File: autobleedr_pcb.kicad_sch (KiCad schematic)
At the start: 21 parts, among them J1 Barrel_Jack, J10 XT60 Connector, J11 Conn_01x02_Pin, J13 Screw_Terminal_01x08, J2 Conn_01x01_Pin, J4 Conn_01x13_Pin, J5 Conn_01x13_Pin, J7 Screw_Terminal_01x02, J8 Conn_01x02_Pin, J9 Conn_01x02_Pin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

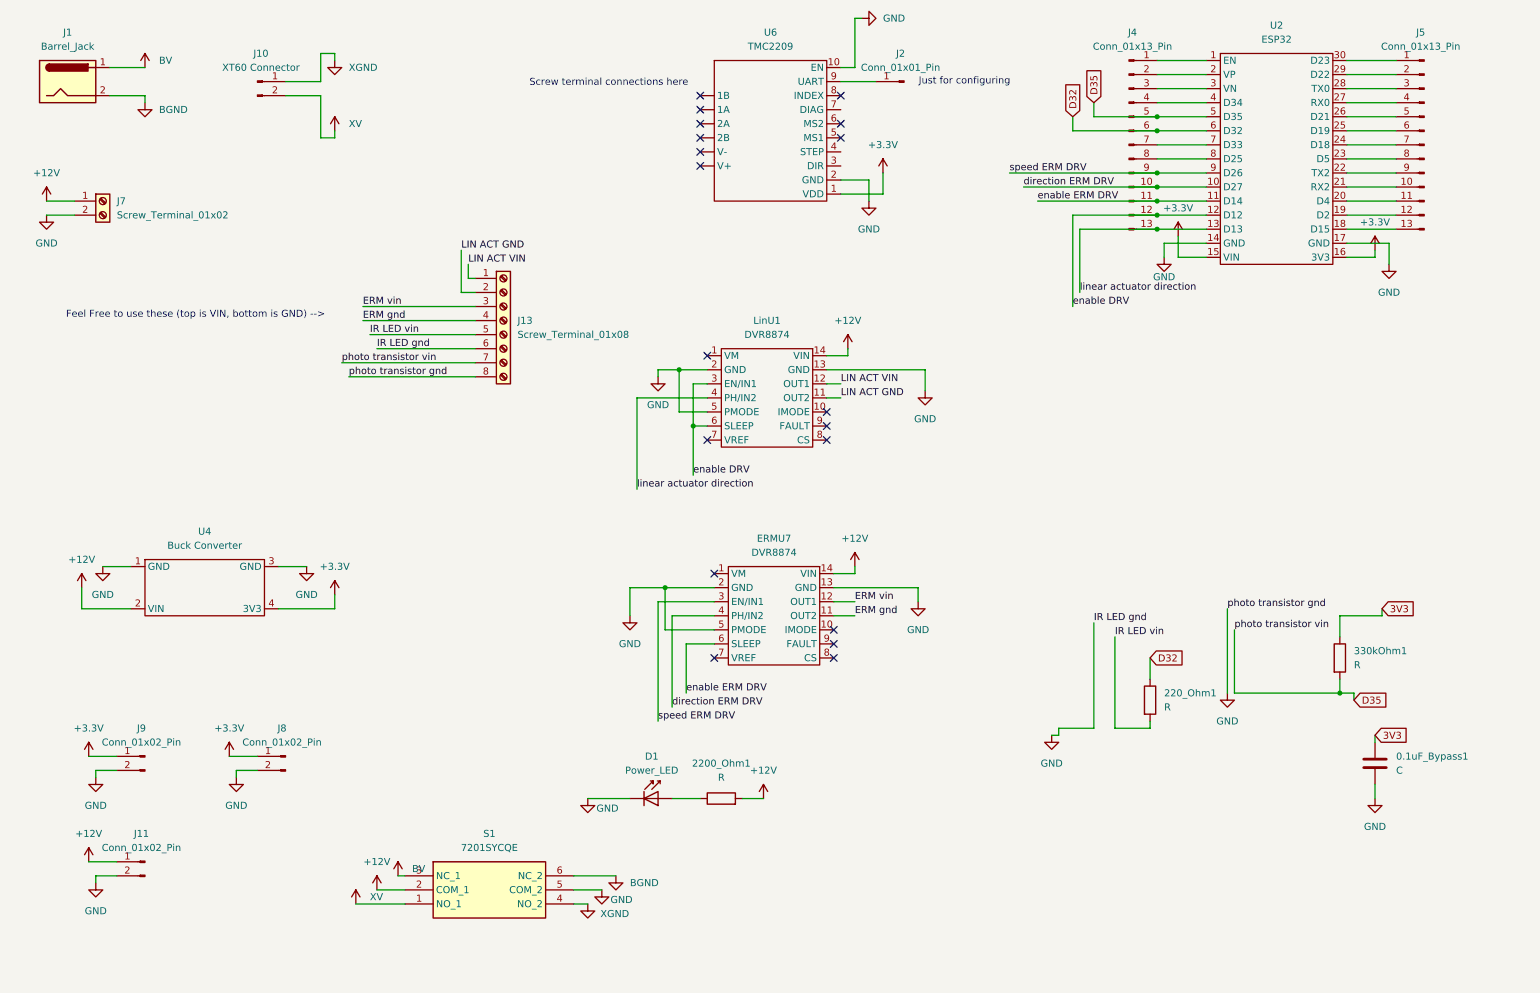
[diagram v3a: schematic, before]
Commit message: added most traces
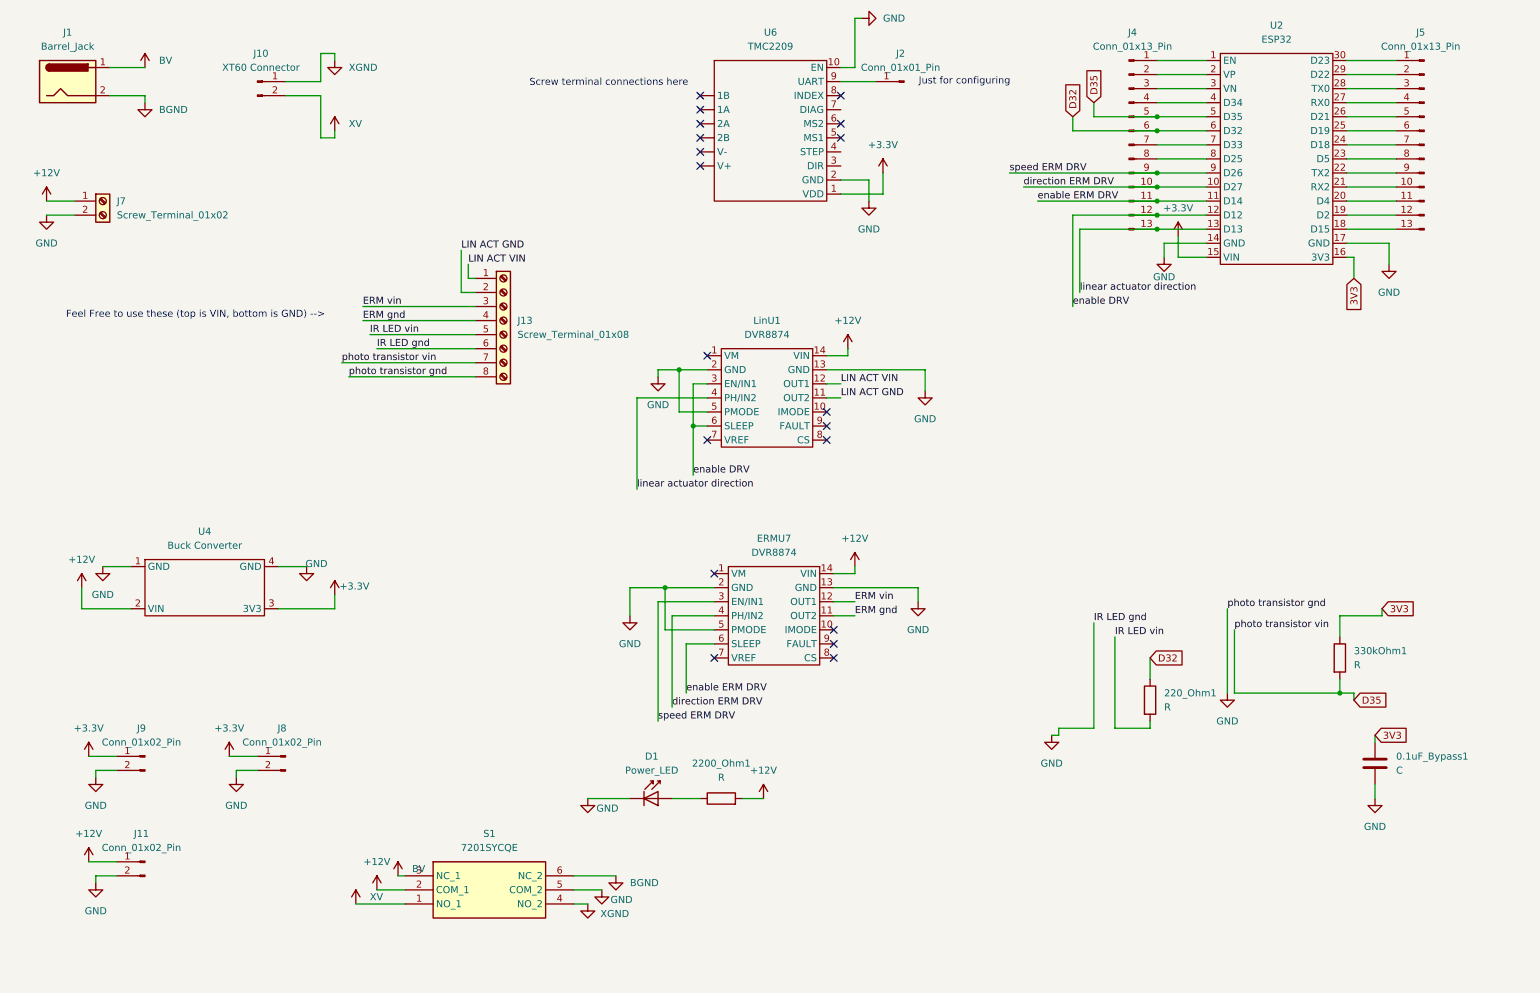
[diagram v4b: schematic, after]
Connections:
- net +3.3V: now also U4.3 (3V3); no longer U2.16 (3V3), U4.4 (3V3)
- net 3V3: now also U2.16 (3V3)
- net GND: now also U4.4 (GND); no longer U4.3 (GND)
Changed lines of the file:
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@@
 	(wire
 		(pts
-			(xy 255.27 62.23) (xy 260.35 62.23)
+			(xy 255.27 62.23) (xy 256.54 62.23)
 		)
 		(stroke
@@
 	(wire
 		(pts
+			(xy 256.54 62.23) (xy 256.54 66.04)
+		)
+		(stroke
+			(width 0)
+			(type default)
+		)
+	)
+	(wire
+		(pts
 			(xy 209.55 34.29) (xy 209.55 36.83)
 		)
@@
 	(wire
 		(pts
-			(xy 260.35 62.23) (xy 260.35 60.96)
-		)
-		(stroke
-			(width 0)
-			(type default)
-		)
-	)
-	(wire
-		(pts
 			(xy 171.45 50.8) (xy 171.45 46.99)
 		)
@@
 		)
 	)
+	(global_label "3V3"
+		(shape input)
+		(at 256.54 66.04 270)
+		(fields_autoplaced yes)
+		(effects
+			(font
+				(size 1.27 1.27)
+			)
+			(justify right)
+		)
+		(property "Intersheetrefs" "${INTERSHEET_REFS}"
+			(at 256.54 72.5328 90)
+			(effects
+				(font
+					(size 1.27 1.27)
+				)
+				(justify right)
+				(hide yes)
+			)
+		)
+	)
 	(global_label "D35"
 		(shape input)
@@
 		(on_board yes)
 		(dnp no)
-		(fields_autoplaced yes)
 		(property "Reference" "#PWR05"
 			(at 67.31 124.46 0)
@@
 		)
 		(property "Value" "GND"
-			(at 67.31 123.19 0)
+			(at 69.088 117.602 0)
 			(effects
 				(font
@@
 	)
 	(symbol
-		(lib_id "power:+3.3V")
-		(at 260.35 60.96 0)
-		(unit 1)
-		(exclude_from_sim no)
-		(in_bom yes)
-		(on_board yes)
-		(dnp no)
-		(property "Reference" "#PWR011"
-			(at 260.35 64.77 0)
-			(effects
-				(font
-					(size 1.27 1.27)
-				)
-				(hide yes)
-			)
-		)
-		(property "Value" "+3.3V"
-			(at 260.35 55.88 0)
-			(effects
-				(font
-					(size 1.27 1.27)
-				)
-			)
-		)
-		(property "Footprint" ""
-			(at 260.35 60.96 0)
-			(effects
-				(font
-					(size 1.27 1.27)
-				)
-				(hide yes)
-			)
-		)
-		(property "Datasheet" ""
-			(at 260.35 60.96 0)
-			(effects
-				(font
-					(size 1.27 1.27)
-				)
-				(hide yes)
-			)
-		)
-		(property "Description" "Power symbol creates a global label with name \"+3.3V\""
-			(at 260.35 60.96 0)
-			(effects
-				(font
-					(size 1.27 1.27)
-				)
-				(hide yes)
-			)
-		)
-		(pin "1"
-		)
-		(instances
-			(project "autobleedr_pcb"
-				(path "/1cb070e6-4268-4590-be3a-70f1be021dfd"
-					(reference "#PWR011")
-					(unit 1)
-				)
-			)
-		)
-	)
-	(symbol
 		(lib_id "power:GND")
 		(at 130.81 83.82 0)
@@
 		(on_board yes)
 		(dnp no)
-		(fields_autoplaced yes)
 		(property "Reference" "#PWR030"
 			(at 72.39 127 0)
@@
 		)
 		(property "Value" "+3.3V"
-			(at 72.39 118.11 0)
+			(at 75.946 121.666 0)
 			(effects
 				(font

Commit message: Rerouted board and changed some gpio pins, added 3.3 led
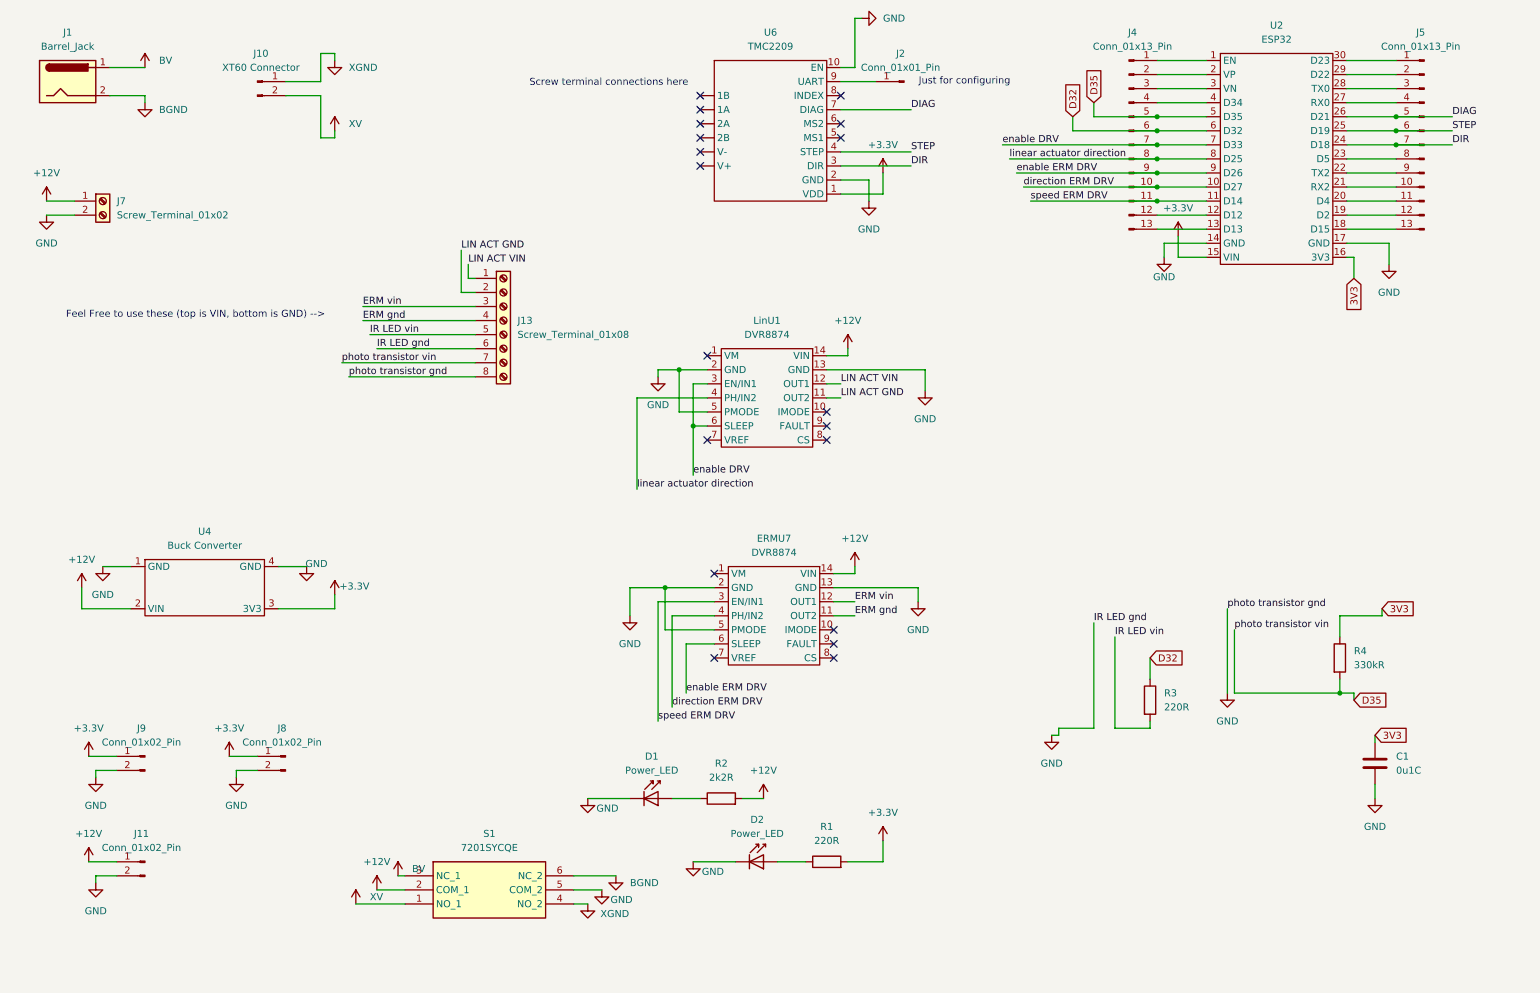
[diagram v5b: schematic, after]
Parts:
- added D2: Power_LED, LED_THT:LED_D5.0mm_IRGrey, symbol LED:CQY99
- added R1: 220R, Resistor_THT:R_Axial_DIN0207_L6.3mm_D2.5mm_P7.62mm_Horizontal, symbol Device:R
- C1: renamed from 0.1uF_Bypass1; value C -> 0u1C
- R2: renamed from 2200_Ohm1; value R -> 2k2R
- R3: renamed from 220_Ohm1; value R -> 220R
- R4: renamed from 330kOhm1; value R -> 330kR
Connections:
- net +3.3V: now also R1.2
- net GND: now also D2.1 (K)
- net enable DRV: now also J4.7 (Pin_7), U2.7 (D33); no longer J4.12 (Pin_12), U2.12 (D12)
- net enable ERM DRV: now also J4.9 (Pin_9), U2.9 (D26); no longer J4.11 (Pin_11), U2.11 (D14)
- net linear actuator direction: now also J4.8 (Pin_8), U2.8 (D25); no longer J4.13 (Pin_13), U2.13 (D13)
- net speed ERM DRV: now also J4.11 (Pin_11), U2.11 (D14); no longer J4.9 (Pin_9), U2.9 (D26)
- net DIR: now reaches U6.3 (DIR)
- net DIR: now also J5.7 (Pin_7), U2.24 (D18)
- net STEP: now reaches U6.4 (STEP)
- net STEP: now also J5.6 (Pin_6), U2.25 (D19)
- net DIAG: now reaches U6.7 (DIAG)
- net DIAG: now also J5.5 (Pin_5), U2.26 (D21)
- new net: J4.12 (Pin_12), U2.12 (D12)
- new net: J4.13 (Pin_13), U2.13 (D13)
- new net: D2.2 (A), R1.1

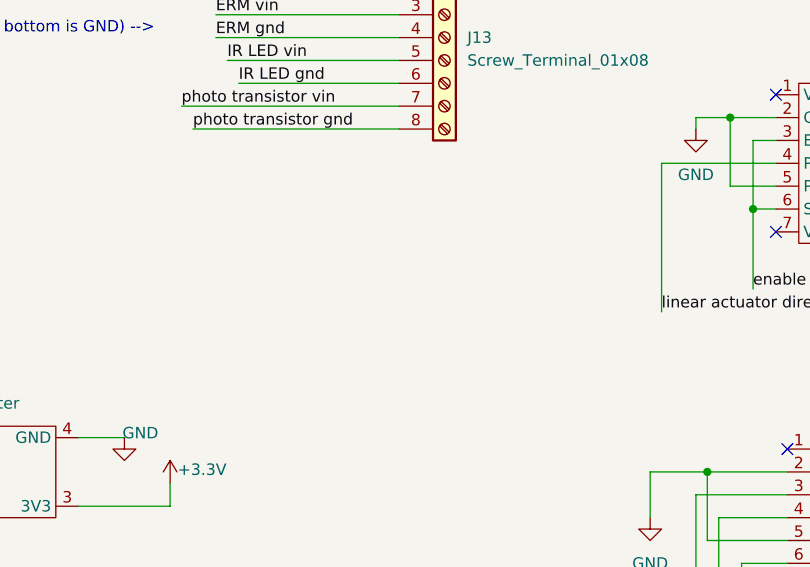
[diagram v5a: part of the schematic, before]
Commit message: Added bulk capacitors
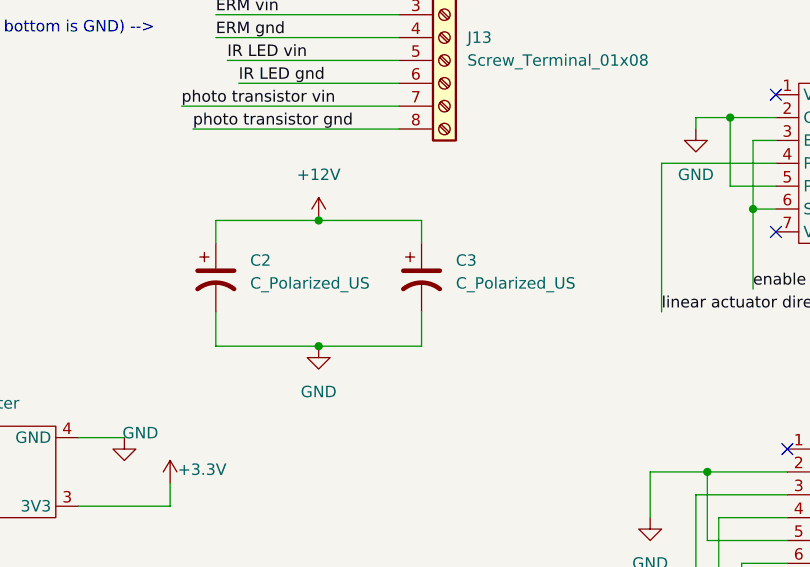
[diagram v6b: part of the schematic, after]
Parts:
- added C2, C3: C_Polarized_US, Capacitor_THT:CP_Radial_D8.0mm_P5.00mm, symbol Device:C_Polarized_US
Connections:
- net +12V: now also C2.1, C3.1
- net GND: now also C2.2, C3.2

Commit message: Made some changes for Barnes
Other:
- note removed: "Feel Free to use these (top is VIN, bottom is GND) -->"
- moved on the sheet: C1, C2, C3, D1, D2, J11, J13, J4, J5, J8, J9, R1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

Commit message: updated v2
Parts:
- removed J1: Barrel_Jack, Connector_BarrelJack:BarrelJack_CUI_PJ-063AH_Horizontal, symbol Connector:Barrel_Jack
- removed J10: XT60 Connector, Connector_AMASS:AMASS_XT60PW-F_1x02_P7.20mm_Horizontal, symbol Connector:Conn_01x02_Pin
- removed J4, J5: Conn_01x13_Pin, Connector_PinHeader_2.54mm:PinHeader_1x13_P2.54mm_Vertical, symbol Connector:Conn_01x13_Pin
- removed J8, J9: Conn_01x02_Pin, Connector_PinHeader_2.54mm:PinHeader_1x02_P2.54mm_Vertical, symbol Connector:Conn_01x02_Pin
- removed S1: 7201SYCQE, 7201SYCQE, symbol Select_Battery_Switch:7201SYCQE
- removed U4: Buck Converter, Capstone_Footprints:Buck_Converter, symbol Capstone_Symbols:Buck_Converter
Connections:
- net 3V3 is gone; now on net +3.3V: C1.1, R4.1, U2.16 (3V3)
- net +3.3V: no longer U2.15 (VIN)
- net +12V renamed +7.4V
- net +7.4V: now also U2.15 (VIN)
- no-connect marks 19 -> 35
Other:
- moved on the sheet: J11
